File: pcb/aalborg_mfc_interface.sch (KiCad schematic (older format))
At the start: 32 parts, among them J1 DB15FV, J2 DB15FV, J3 DB15FV, P1 PWR_JACK_2.5x5.5, P2 HEADER_01X03, P3 BNC_DOUBLE_RA, P4 HEADER_01X03_SHR, P5 HEADER_01X03_SHR, P6 HEADER_01X03_SHR, SW1 SPST_SERIES_M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

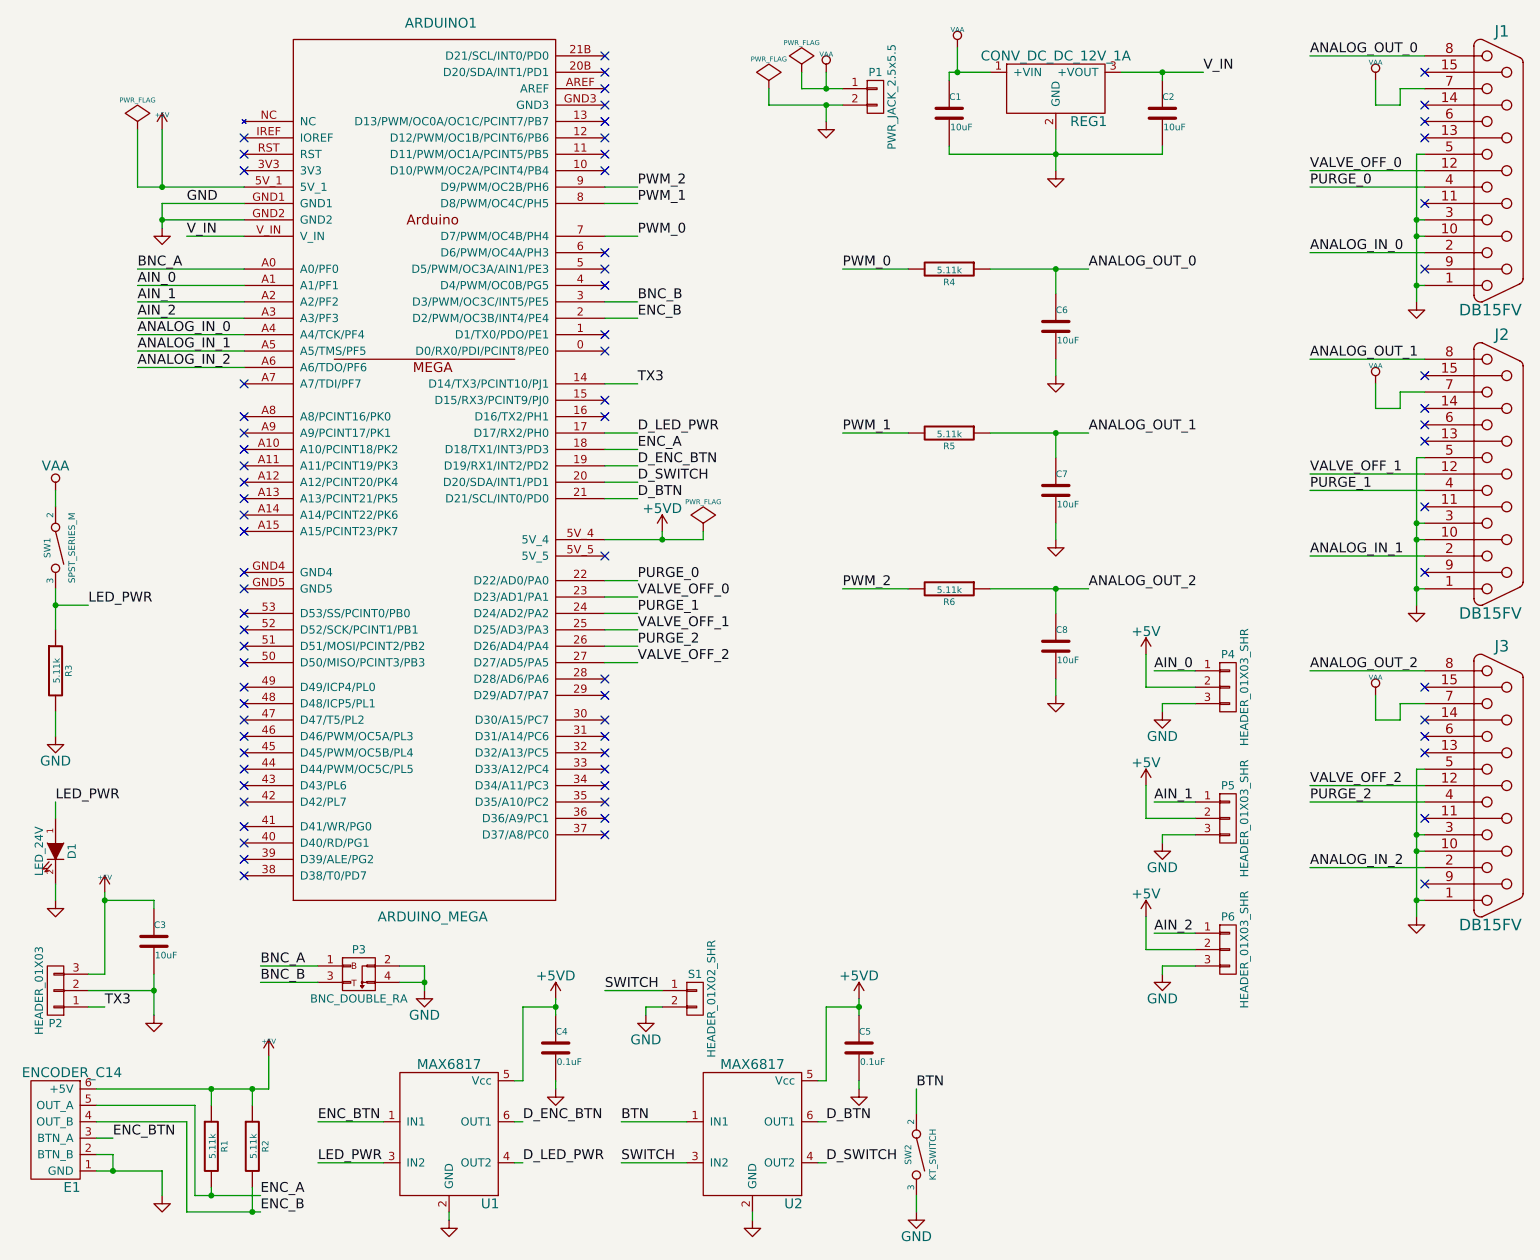
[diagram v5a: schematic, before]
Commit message: SPST switch -> DPST switch.
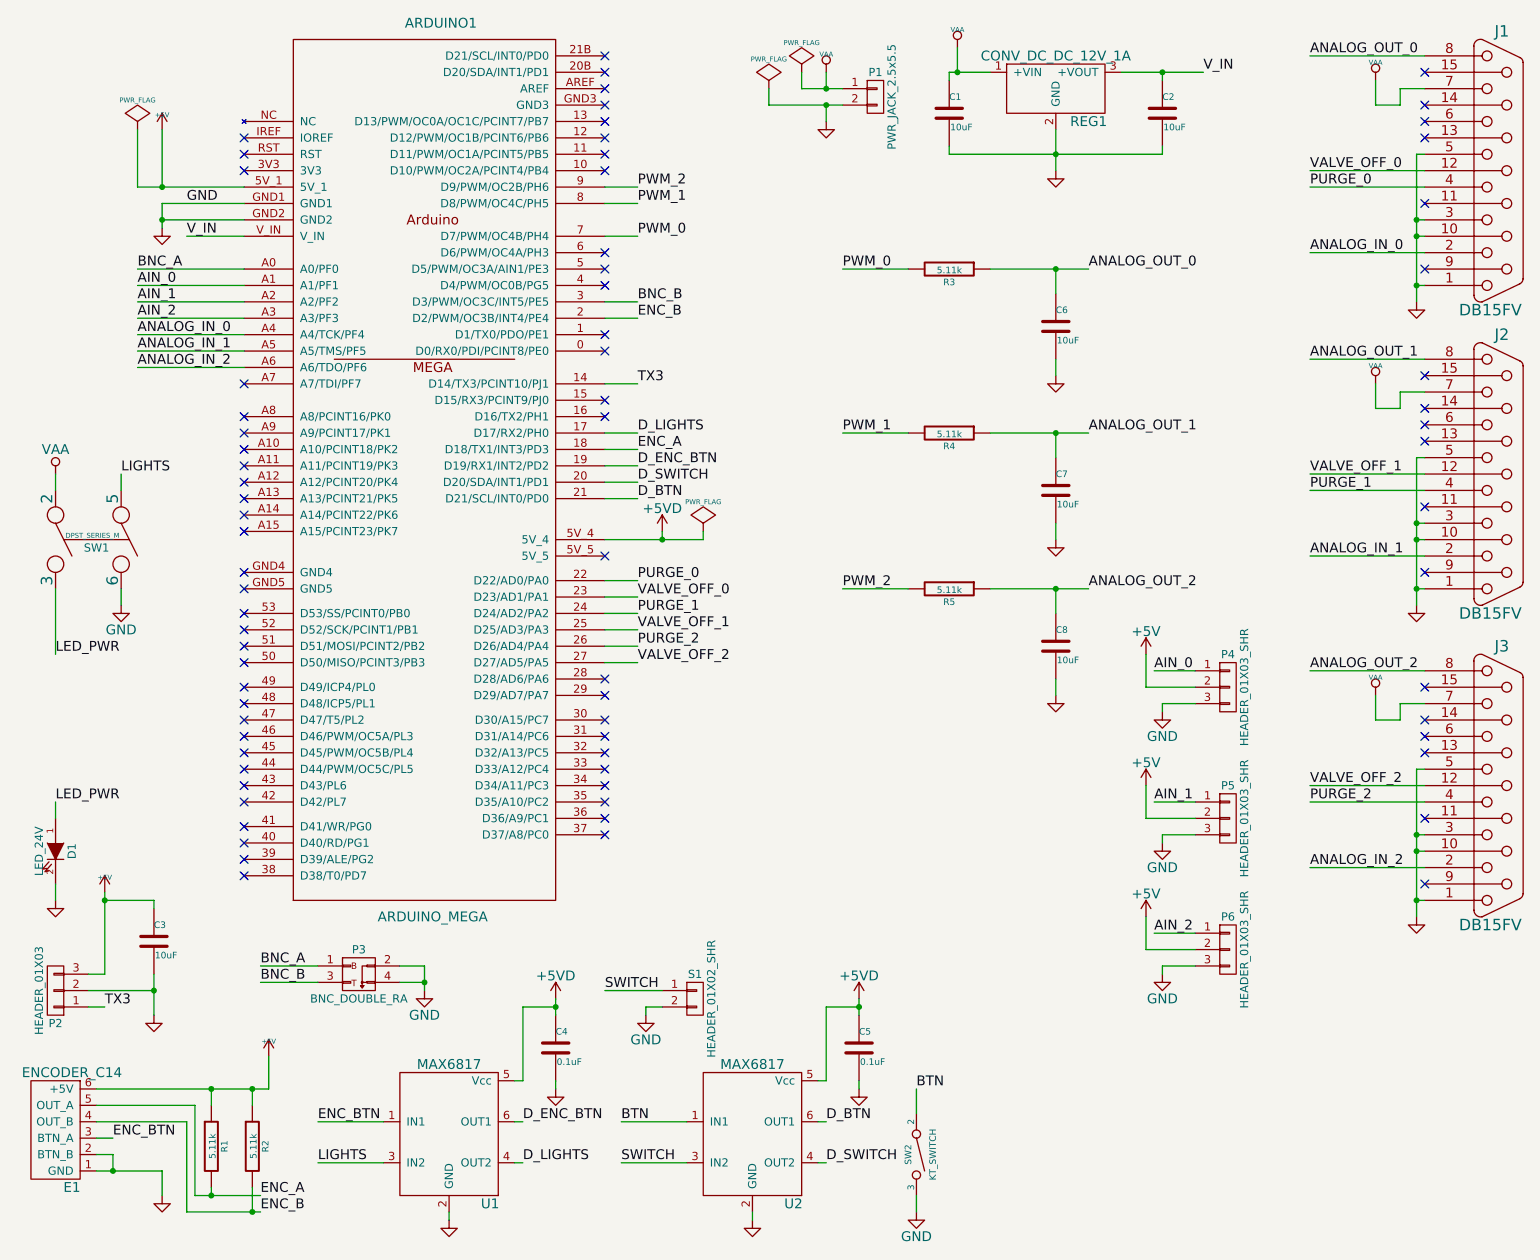
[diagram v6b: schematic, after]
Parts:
- removed R3: 5.11k, aalborg_mfc_interface:SM1210, symbol 5.11k
- removed SW1: SPST_SERIES_M, aalborg_mfc_interface:SPST_SERIES_M, symbol SPST_SERIES_M
- added SW1: DPST_SERIES_M, aalborg_mfc_interface:DPST_SERIES_M, symbol DPST_SERIES_M
- renumbered R4 to R3, R5 to R4, R6 to R5
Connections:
- net GND: now also SW1.6
- net LED_PWR: now also SW1.3; no longer U1.3 (IN2)
- net VAA: now also SW1.2
- net D_LED_PWR renamed D_LIGHTS
- new net LIGHTS: SW1.5, U1.3 (IN2)
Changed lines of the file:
@@
 LIBS:memory
 LIBS:xilinx
-LIBS:special
 LIBS:microcontrollers
 LIBS:dsp
@@
 LIBS:valves
 LIBS:aalborg_mfc_interface
+LIBS:components
 LIBS:aalborg_mfc_interface-cache
 EELAYER 25 0
@@
 Title "aalborg_mfc_interface"
 Date ""
-Rev "1.2"
+Rev "1.3"
 Comp "Janelia"
 Comment1 ""
@@
 NoConn ~ 4050 2450
 NoConn ~ 4050 2550
-NoConn ~ 4050 2850
 NoConn ~ 4050 2950
 NoConn ~ 4050 3800
@@
 $EndComp
 $Comp
-L 5.11k R4
+L 5.11k R3
 U 1 1 54894188
 P 6150 2050
-F 0 "R4" V 6230 2050 40  0000 C CNN
+F 0 "R3" V 6230 2050 40  0000 C CNN
 F 1 "5.11k" V 6157 2051 40  0000 C CNN
 F 2 "aalborg_mfc_interface:SM1210" V 6080 2050 30  0001 C CNN
@@
 $EndComp
 $Comp
-L 5.11k R5
+L 5.11k R4
 U 1 1 5489443F
 P 6150 3050
-F 0 "R5" V 6230 3050 40  0000 C CNN
+F 0 "R4" V 6230 3050 40  0000 C CNN
 F 1 "5.11k" V 6157 3051 40  0000 C CNN
 F 2 "aalborg_mfc_interface:SM1210" V 6080 3050 30  0001 C CNN
@@
 	4050 3150 4250 3150
 Text Label 4250 3050 0    60   ~ 0
-D_LED_PWR
+D_LIGHTS
 Text Label 700  5300 0    60   ~ 0
 LED_PWR
@@
 	2700 7500 2300 7500
 Text Label 2300 7500 0    60   ~ 0
-LED_PWR
+LIGHTS
 Wire Wire Line
 	3500 7500 3550 7500
 Text Label 3550 7500 0    60   ~ 0
-D_LED_PWR
+D_LIGHTS
 $Comp
 L VAA #PWR023
 U 1 1 54AF28AD
-P 700 3400
-F 0 "#PWR023" H 700 3250 60  0001 C CNN
-F 1 "VAA" H 700 3550 60  0000 C CNN
-F 2 "" H 700 3400 60  0000 C CNN
-F 3 "" H 700 3400 60  0000 C CNN
-	1    700  3400
-	1    0    0    -1
-$EndComp
-$Comp
-L 5.11k R3
-U 1 1 54AF2C25
-P 700 4500
-F 0 "R3" V 780 4500 40  0000 C CNN
-F 1 "5.11k" V 707 4501 40  0000 C CNN
-F 2 "aalborg_mfc_interface:SM1210" V 630 4500 30  0001 C CNN
-F 3 "" H 700 4500 30  0000 C CNN
-F 4 "digikey" V 880 4600 60  0001 C CNN "Vendor"
-F 5 "P5.11KAACT-ND" V 980 4700 60  0001 C CNN "PartNumber"
-F 6 "RES SMD 5.11K OHM 1% 1/2W 1210" V 1080 4800 60  0001 C CNN "Description"
-	1    700  4500
+P 700 3300
+F 0 "#PWR023" H 700 3150 60  0001 C CNN
+F 1 "VAA" H 700 3450 60  0000 C CNN
+F 2 "" H 700 3300 60  0000 C CNN
+F 3 "" H 700 3300 60  0000 C CNN
+	1    700  3300
 	1    0    0    -1
 $EndComp
@@
 L GND #PWR024
 U 1 1 54AF2C77
-P 700 4900
-F 0 "#PWR024" H 700 4650 60  0001 C CNN
-F 1 "GND" H 700 4750 60  0000 C CNN
-F 2 "" H 700 4900 60  0000 C CNN
-F 3 "" H 700 4900 60  0000 C CNN
-	1    700  4900
-	1    0    0    -1
-$EndComp
-Wire Wire Line
-	700  4000 700  4250
-Wire Wire Line
-	700  4750 700  4900
-Wire Wire Line
-	700  4100 900  4100
-Connection ~ 700  4100
-Text Label 900  4100 0    60   ~ 0
+P 1100 4100
+F 0 "#PWR024" H 1100 3850 60  0001 C CNN
+F 1 "GND" H 1100 3950 60  0000 C CNN
+F 2 "" H 1100 4100 60  0000 C CNN
+F 3 "" H 1100 4100 60  0000 C CNN
+	1    1100 4100
+	1    0    0    -1
+$EndComp
+Text Label 700  4400 0    60   ~ 0
 LED_PWR
 $Comp
@@
 $EndComp
 $Comp
-L 5.11k R6
+L 5.11k R5
 U 1 1 54B44545
 P 6150 4000
-F 0 "R6" V 6230 4000 40  0000 C CNN
+F 0 "R5" V 6230 4000 40  0000 C CNN
 F 1 "5.11k" V 6157 4001 40  0000 C CNN
 F 2 "aalborg_mfc_interface:SM1210" V 6080 4000 30  0001 C CNN
@@
 Wire Wire Line
 	4300 6550 4400 6550
-$Comp
-L SPST_SERIES_M SW1
-U 1 1 54B9764F
-P 700 3750
-F 0 "SW1" H 700 3700 40  0000 C CNN
-F 1 "SPST_SERIES_M" H 700 3850 40  0000 C CNN
-F 2 "aalborg_mfc_interface:SPST_SERIES_M" H 600 3550 60  0001 C CNN
-F 3 "" H 700 3750 60  0000 C CNN
-F 4 "digikey" H 800 3950 60  0001 C CNN "Vendor"
-F 5 "360-3243-ND" H 900 4050 60  0001 C CNN "PartNumber"
-F 6 "SWITCH TOGGLE SPST 6A 125V" H 1000 4150 60  0001 C CNN "Description"
-	1    700  3750
-	0    1    1    0
-$EndComp
-Wire Wire Line
-	700  3400 700  3500
 Wire Wire Line
 	4050 3350 4250 3350
@@
 	1    0    0    -1
 $EndComp
-Wire Wire Line
-	4050 3050 4250 3050
 Text Label 4250 3150 0    60   ~ 0
 ENC_A
@@
 Text Label 1950 6400 0    60   ~ 0
 BNC_B
+Wire Wire Line
+	700  3400 700  3300
+Wire Wire Line
+	1100 3300 1100 3400
+$Comp
+L DPST_SERIES_M SW1
+U 1 1 55C8DAA5
+P 900 3700
+F 0 "SW1" V 950 3750 50  0000 C CNN
+F 1 "DPST_SERIES_M" V 875 3725 30  0000 C CNN
+F 2 "aalborg_mfc_interface:DPST_SERIES_M" H 1100 3650 60  0001 C CNN
+F 3 "" H 1200 3750 60  0000 C CNN
+F 4 "digikey" H 1300 3850 60  0001 C CNN "Vendor"
+F 5 "360-3244-ND" H 1400 3950 60  0001 C CNN "PartNumber"
+F 6 "SWITCH TOGGLE DPST 6A 125V" H 1500 4050 60  0001 C CNN "Description"
+	1    900  3700
+	0    1    1    0
+$EndComp
+Text Label 1100 3300 0    60   ~ 0
+LIGHTS
+NoConn ~ 4050 2850
+Wire Wire Line
+	4050 3050 4250 3050
+Wire Wire Line
+	1100 4000 1100 4100
+Wire Wire Line
+	700  4000 700  4400
 $EndSCHEMATC
